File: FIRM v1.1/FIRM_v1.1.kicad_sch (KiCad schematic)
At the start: 89 parts, among them J2 Conn_01x02_Pin, Q1 IRLML6402, U10 STM32F446ZCHx, U3 ADXL371, U5 INA219AxDCN, U6 MIC5219-3.3YM5, U9 A-USBC-20F0-EA-GSR05, Y2 12 MHz

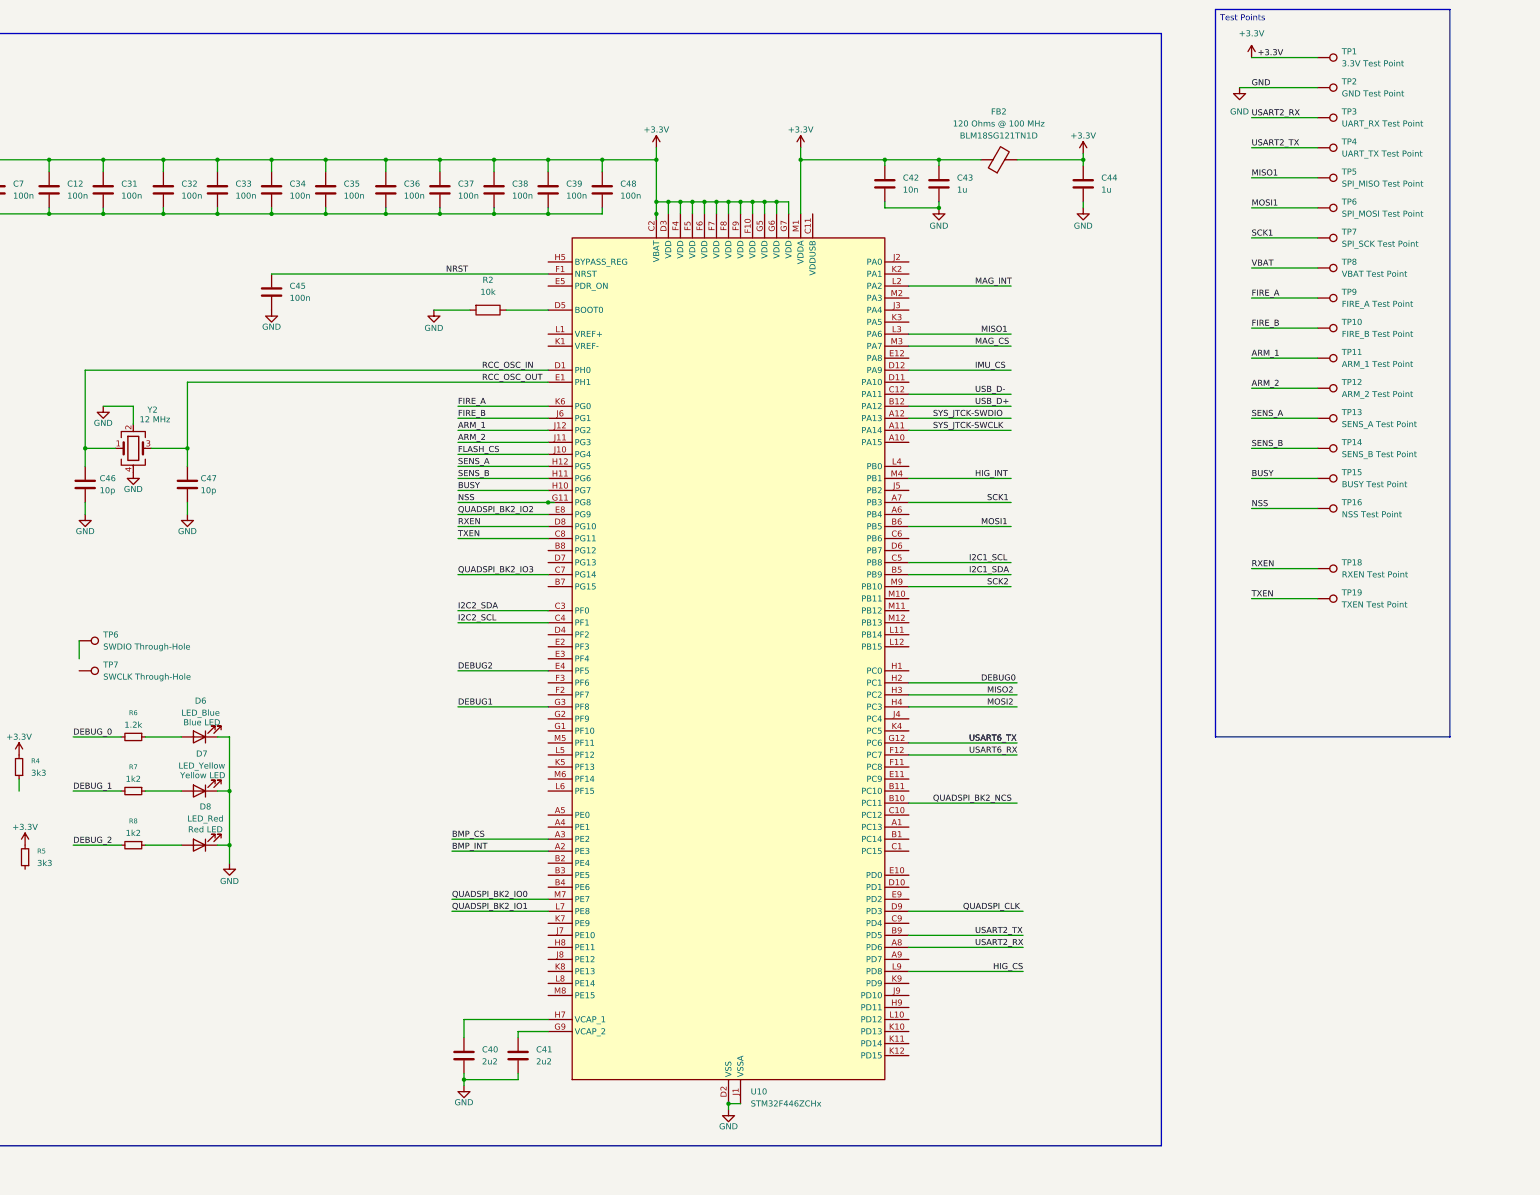
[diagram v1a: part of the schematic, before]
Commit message: Finished Pinout for STM
Fixed Pin out and test Pins
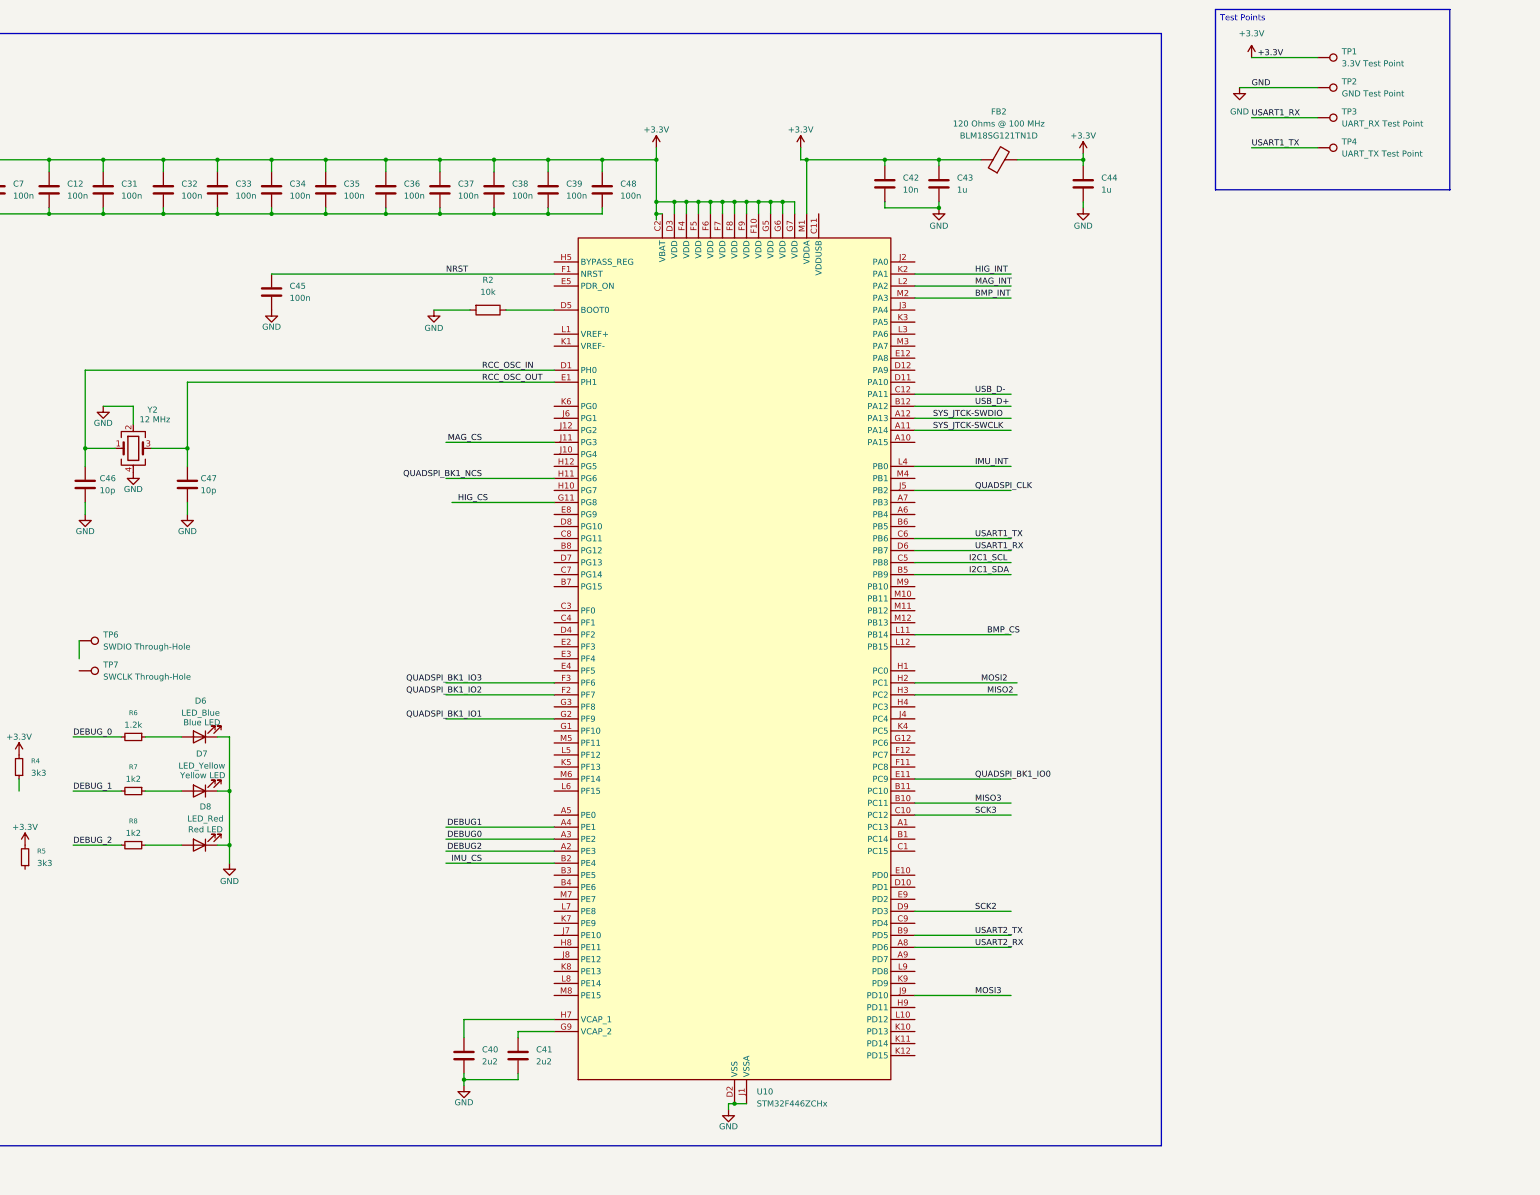
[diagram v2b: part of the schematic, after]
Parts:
- removed TP10: FIRE_B Test Point, connectors:Testpoint_1.5x1.5mm_1.0mm, symbol Connector:TestPoint
- removed TP11: ARM_1 Test Point, connectors:Testpoint_1.5x1.5mm_1.0mm, symbol Connector:TestPoint
- removed TP12: ARM_2 Test Point, connectors:Testpoint_1.5x1.5mm_1.0mm, symbol Connector:TestPoint
- removed TP13: SENS_A Test Point, connectors:Testpoint_1.5x1.5mm_1.0mm, symbol Connector:TestPoint
- removed TP14: SENS_B Test Point, connectors:Testpoint_1.5x1.5mm_1.0mm, symbol Connector:TestPoint
- removed TP15: BUSY Test Point, connectors:Testpoint_1.5x1.5mm_1.0mm, symbol Connector:TestPoint
- removed TP16: NSS Test Point, connectors:Testpoint_1.5x1.5mm_1.0mm, symbol Connector:TestPoint
- removed TP18: RXEN Test Point, connectors:Testpoint_1.5x1.5mm_1.0mm, symbol Connector:TestPoint
- removed TP19: TXEN Test Point, connectors:Testpoint_1.5x1.5mm_1.0mm, symbol Connector:TestPoint
- removed TP5: SPI_MISO Test Point, connectors:Testpoint_1.5x1.5mm_1.0mm, symbol Connector:TestPoint
- removed TP6: SPI_MOSI Test Point, connectors:Testpoint_1.5x1.5mm_1.0mm, symbol Connector:TestPoint
- removed TP7: SPI_SCK Test Point, connectors:Testpoint_1.5x1.5mm_1.0mm, symbol Connector:TestPoint
- removed TP8: VBAT Test Point, connectors:Testpoint_1.5x1.5mm_1.0mm, symbol Connector:TestPoint
- removed TP9: FIRE_A Test Point, connectors:Testpoint_1.5x1.5mm_1.0mm, symbol Connector:TestPoint
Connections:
- net ARM_2 is gone; now on net MAG_CS: U10.J11 (PG3)
- net NSS is gone; now on net HIG_CS: U10.G11 (PG8)
- net SENS_B is gone; now on net QUADSPI_BK1_NCS: U10.H11 (PG6)
- net BMP_CS: now also U10.L11 (PB14); no longer U10.A3 (PE2)
- net BMP_INT: now also U10.M2 (PA3); no longer U10.A2 (PE3)
- net DEBUG0: now also U10.A3 (PE2); no longer U10.H2 (PC1)
- net DEBUG1: now also U10.A4 (PE1); no longer U10.G3 (PF8)
- net DEBUG2: now also U10.A2 (PE3); no longer U10.E4 (PF5)
- net HIG_CS: no longer U10.L9 (PD8)
- net HIG_INT: now also U10.K2 (PA1); no longer U10.M4 (PB1)
- net IMU_CS: now also U10.B2 (PE4); no longer U10.D12 (PA9)
- net IMU_INT: now also U10.L4 (PB0)
- net MAG_CS: no longer U10.M3 (PA7)
- net MOSI2: now also U10.H2 (PC1); no longer U10.H4 (PC3)
- net QUADSPI_BK1_IO0: now also U10.E11 (PC9)
- net QUADSPI_BK1_IO1: now also U10.G2 (PF9)
- net QUADSPI_BK1_IO2: now also U10.F2 (PF7)
- net QUADSPI_BK1_IO3: now also U10.F3 (PF6)
- net QUADSPI_CLK: now also U10.J5 (PB2); no longer U10.D9 (PD3)
- net SCK2: now also U10.D9 (PD3); no longer U10.M9 (PB10)
- net USART2_RX: no longer TP3.1
- net USART2_TX: no longer TP4.1
- net SCK3: now reaches U10.C10 (PC12)
- net USART1_TX: now reaches U10.C6 (PB6)
- net USART1_TX: now also TP4.1
- net USART1_RX: now reaches U10.D6 (PB7)
- net USART1_RX: now also TP3.1
- net MOSI3: now reaches U10.J9 (PD10)
- net ARM_1: no longer names the net of U10.J12 (PG2)
- net BUSY: no longer names the net of U10.H10 (PG7)
- net FIRE_A: no longer names the net of U10.K6 (PG0)
- net FIRE_B: no longer names the net of U10.J6 (PG1)
- net FLASH_CS: no longer names the net of U10.J10 (PG4)
- net I2C2_SCL: no longer names the net of U10.C4 (PF1)
- net I2C2_SDA: no longer names the net of U10.C3 (PF0)
- net MISO1: no longer names the net of U10.L3 (PA6)
- net MOSI1: no longer names the net of U10.B6 (PB5)
- net QUADSPI_BK2_IO0: no longer names the net of U10.M7 (PE7)
- net QUADSPI_BK2_IO1: no longer names the net of U10.L7 (PE8)
- net QUADSPI_BK2_IO2: no longer names the net of U10.E8 (PG9)
- net QUADSPI_BK2_IO3: no longer names the net of U10.C7 (PG14)
- net QUADSPI_BK2_NCS renamed MISO3
- net RXEN: no longer names the net of U10.D8 (PG10)
- net SCK1: no longer names the net of U10.A7 (PB3)
- net SENS_A: no longer names the net of U10.H12 (PG5)
- net TXEN: no longer names the net of U10.C8 (PG11)
- net USART6_RX: no longer names the net of U10.F12 (PC7)
- net USART6_TX: no longer names the net of U10.G12 (PC6)
- new net: U3.10 (RES), U3.13 (GND), U3.16 (GND)
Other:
- moved on the sheet: U10

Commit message: Schematic complete
Everything on the pin out is complete and I have a STM32 Project complete with the correct pin out. I still have concerns regarding the Ferrite bead
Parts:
- added R10, R11, R12, R13, R14: 0, Package_DIP:DIP-8_W7.62mm, symbol Device:R_Small
- added RN1: 10k, Resistor_THT:R_Array_SIP6, symbol Device:R_Pack03
- R1, R3, R9: value 10k -> 0; footprint (none) -> Package_DIP:DIP-8_W7.62mm
- R4, R5: footprint Resistor_SMD:R_0402_1005Metric -> Package_DIP:DIP-8_W7.62mm; Digikey PN P3.3KDCCT-ND -> (none); MPN C22356633 -> (none)
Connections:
- net SYS_JTCK-SWDIO is gone; now on net SYS_JTMS-SWDIO: U10.A12 (PA13)
- net +3.3V: now also U10.E5 (PDR_ON), RN1.1 (R1.1), RN1.2 (R2.1), RN1.3 (R3.1); no longer R1.2, R3.2, R9.2
- net GND: now also U10.H5 (BYPASS_REG)
- net I2C1_SCL: now also R5.1
- net I2C1_SDA: now also R4.1
- net MISO2: now also R3.1; no longer U10.H3 (PC2)
- net MISO3: now also R9.2; no longer U10.B10 (PC11)
- net MOSI2: now also R1.2; no longer U10.H2 (PC1)
- net MOSI3: now also R10.2; no longer U10.J9 (PD10)
- net QUADSPI_BK1_IO0: now also R14.2; no longer U10.E11 (PC9)
- net QUADSPI_BK1_IO1: now also R13.2; no longer U10.G2 (PF9)
- net QUADSPI_BK1_IO2: now also R12.2, RN1.5 (R2.2); no longer R9.1, U10.F2 (PF7)
- net QUADSPI_BK1_IO3: now also R11.1, RN1.6 (R1.2); no longer R3.1, U10.F3 (PF6)
- net QUADSPI_BK1_NCS: now also RN1.4 (R3.2); no longer R1.1
- net SYS_JTCK-SWCLK: now also TP7.1
- net SYS_JTMS-SWDIO: now reaches TP6.1
- new net: R3.2, U10.H3 (PC2)
- new net: R13.1, U10.G2 (PF9)
- new net: R1.1, U10.H2 (PC1)
- new net: R14.1, U10.E11 (PC9)
- new net: R11.2, U10.F3 (PF6)
- new net: R10.1, U10.J9 (PD10)
- new net: R9.1, U10.B10 (PC11)
- new net: R12.1, U10.F2 (PF7)
- new net: U3.10 (RES), U3.13 (GND), U3.16 (GND)
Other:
- moved on the sheet: C1, C19, C20, C21, C22, C23, C24, C25, C26, C27, C28, C29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

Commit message: Slimed out the Ferrite Bead
Took out the ferrite bead and connected to VDD
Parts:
- removed C42: 10n, Capacitor_SMD:C_0402_1005Metric, symbol Device:C
- removed C43, C44: 1u, Capacitor_SMD:C_0402_1005Metric, symbol Device:C
- removed FB2: 120 Ohms @ 100 MHz, Inductor_SMD:L_0603_1608Metric, symbol Device:FerriteBead
- added C8, C9: 100n, Capacitor_SMD:C_0402_1005Metric, symbol Device:C
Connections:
- net +3.3V: now also U10.C11 (VDDUSB), C8.1, C9.1
- net GND: now also C8.2, C9.2
- new net: U3.10 (RES), U3.13 (GND), U3.16 (GND)
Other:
- moved on the sheet: C1, C12, C19, C20, C21, C22, C23, C24, C25, C26, C27, C28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
